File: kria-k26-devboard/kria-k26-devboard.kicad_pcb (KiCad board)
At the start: 2 copper layers, 6 parts, among them J1 ADM6-60-01.5-L-4-2-A-TR, J2 ADM6-60-01.5-L-4-2-A-TR

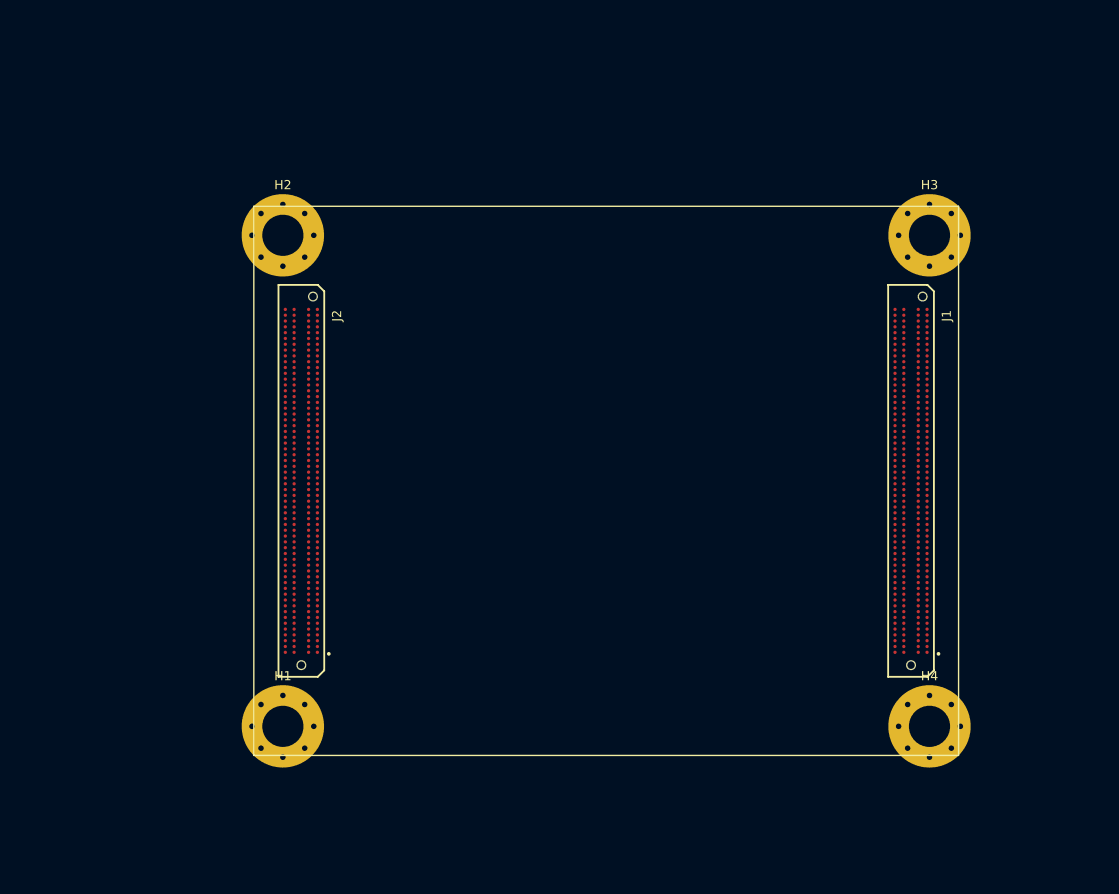
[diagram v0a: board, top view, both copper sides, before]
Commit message: Add dummy connectors for mechanical mockup purpouses
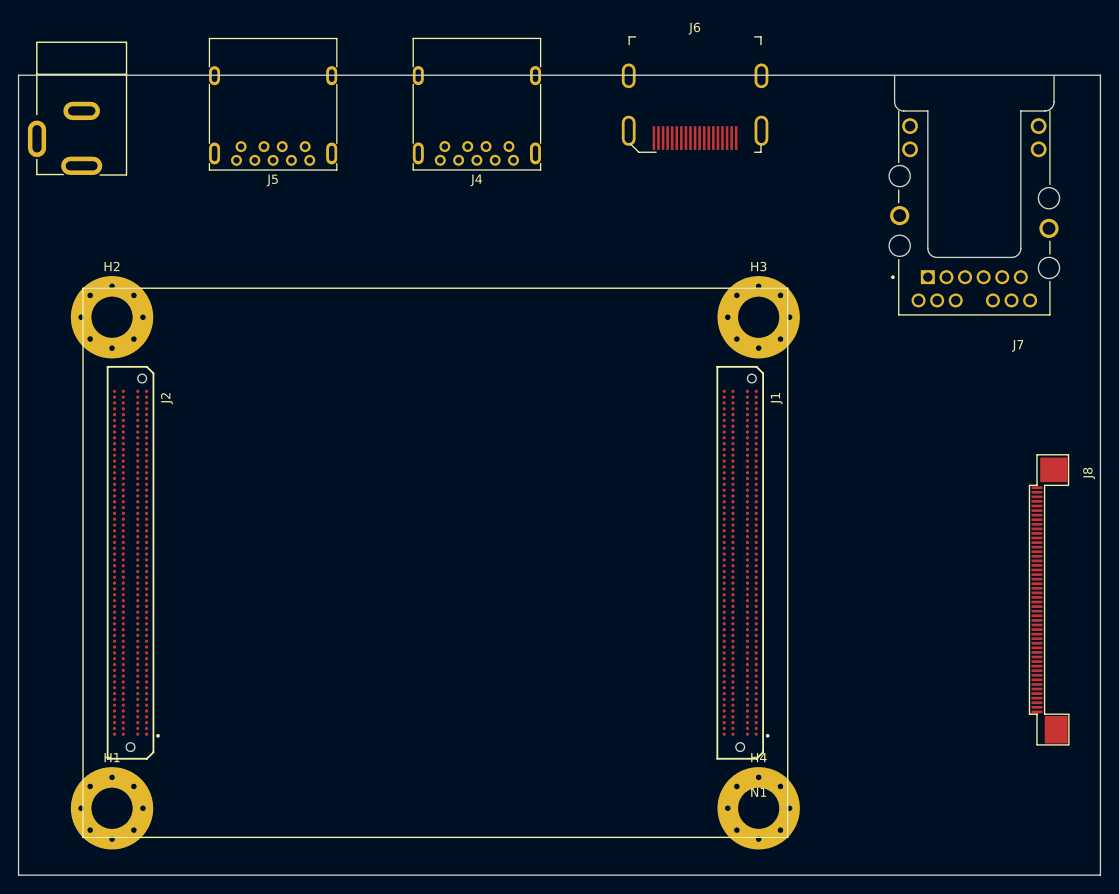
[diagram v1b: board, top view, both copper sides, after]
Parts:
- added J3: DC_SOCKET, antmicro-footprints:DC_SOCKET, F.Cu at (85.8, 43.6)
- added J4: 48393-0001, antmicro-footprints:48393-001, F.Cu at (132.5, 55.2)
- added J5: 48393-0001, antmicro-footprints:48393-001, F.Cu at (110.2, 55.2)
- added J6: 685119134923_, antmicro-footprints:HDMI_A_Female_685119134923, F.Cu at (152.8, 53.0)
- added J7: L834-1G1T-S7, antmicro-footprints:BEL_L834-1G1T-S7, F.Cu at (183.3, 62.8)
- added J8: WE_68715014022, antmicro-footprints:WE_68715014022, F.Cu at (190.8, 105.4)
- added N1: Housing, Fiducial:Fiducial_0.5mm_Mask1.5mm, F.Cu at (159.8, 127.5)
- moved H1 20.7 mm to (89.1, 127.5)
- moved H2 20.7 mm to (89.1, 73.9)
- moved J2 20.7 mm to (91.1, 100.7)
- moved H3 20.7 mm to (159.8, 73.9)
- moved H4 20.7 mm to (159.8, 127.5)
- moved J1 20.7 mm to (157.7, 100.7)
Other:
- board outline added: 118.2 x 87.4 mm

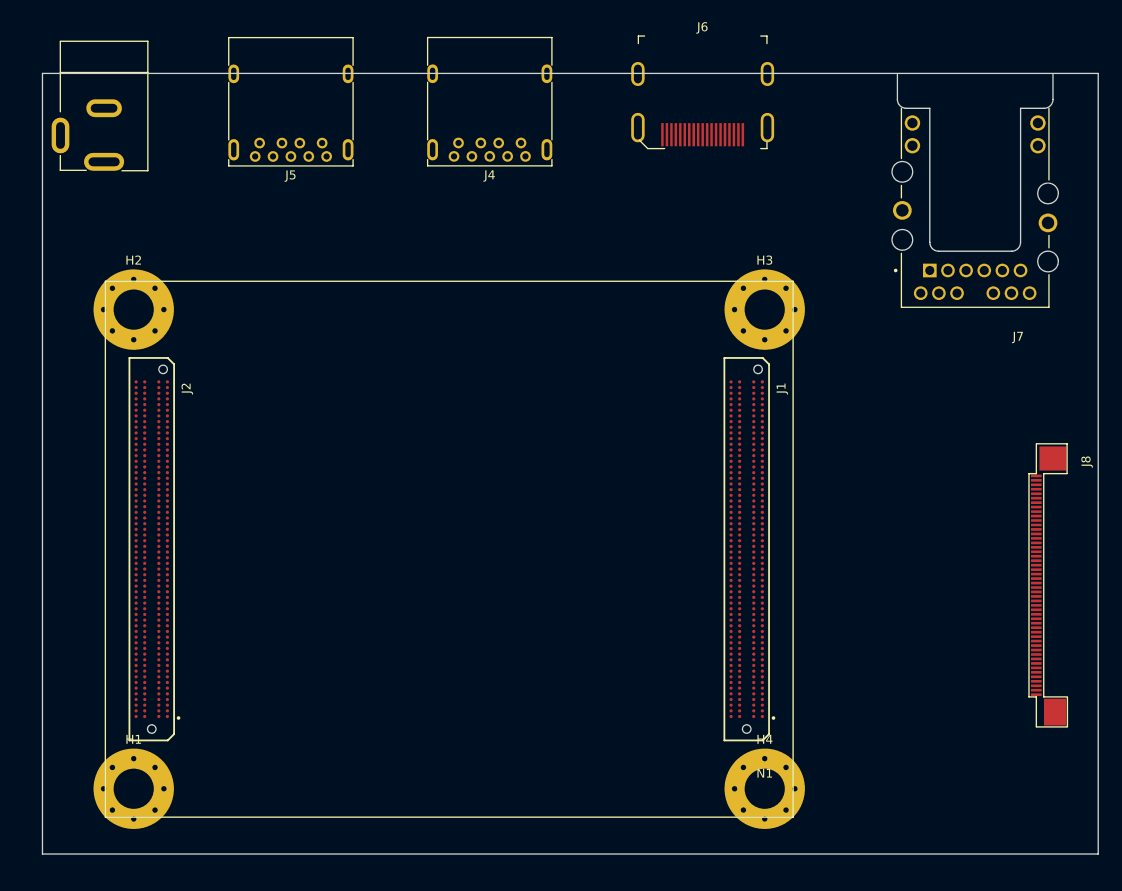
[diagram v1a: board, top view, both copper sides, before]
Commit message: Replace K26 SOM with virtual component
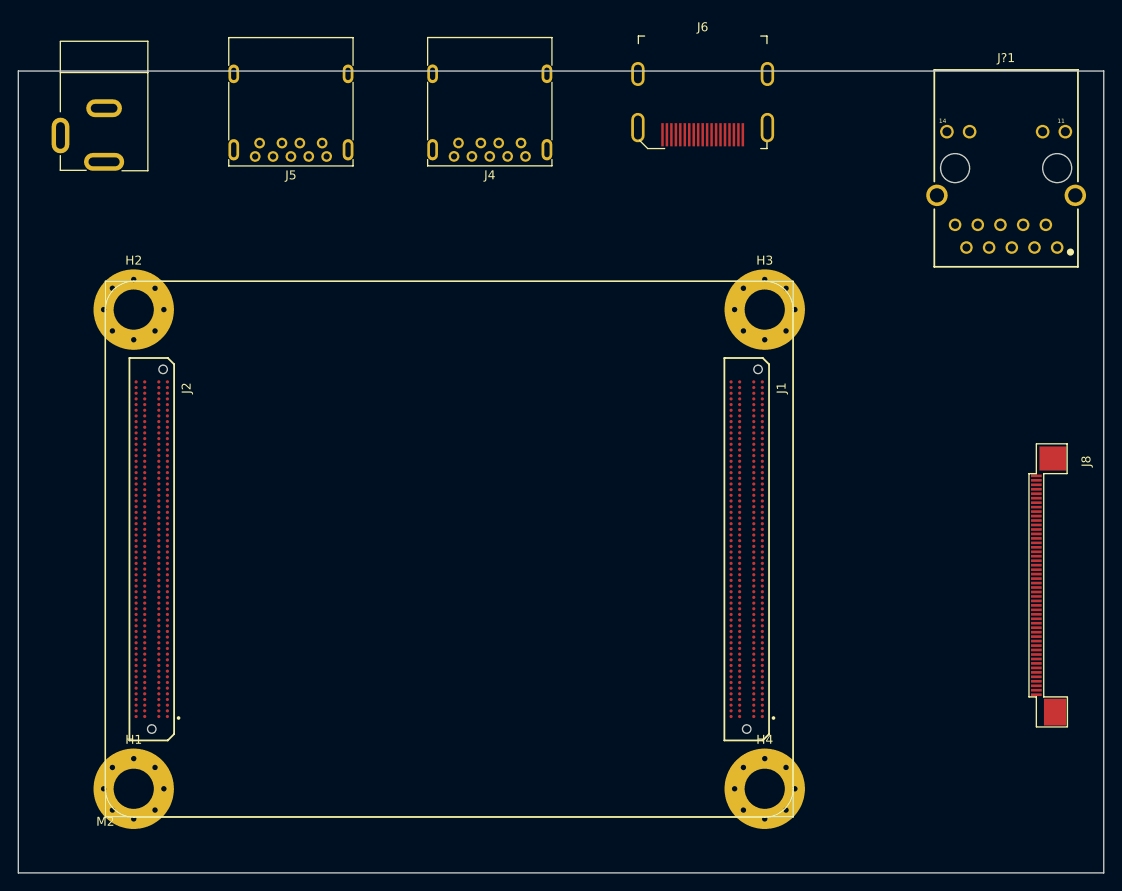
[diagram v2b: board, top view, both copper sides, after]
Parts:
- removed J7: L834-1G1T-S7, antmicro-footprints:BEL_L834-1G1T-S7
- removed N1: Housing, Fiducial:Fiducial_0.5mm_Mask1.5mm
- added J?1: WE-RJ45_7499111121A, antmicro-footprints:7499111121A, F.Cu at (186.8, 58.0)
- added M2: XILINX-KRIA-K26, antmicro-footprints:XILINX-KRIA-K26, F.Cu at (85.9, 130.7)
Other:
- board size 118.2 x 87.4 mm -> 121.5 x 89.8 mm

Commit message: First sketches of POE part of supply
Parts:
- removed H1, H2, H3, H4: MountingHole_Pad, MountingHole:MountingHole_4.5mm_Pad_Via
- removed J8: WE_68715014022, antmicro-footprints:WE_68715014022
- removed J?1: WE-RJ45_7499111121A, antmicro-footprints:7499111121A
- removed M2: XILINX-KRIA-K26, antmicro-footprints:XILINX-KRIA-K26
- added C1: C_47u_0805, antmicro-footprints:0805-cap, F.Cu at (293.3, 60.4)
- added C2: C_47u_0805, antmicro-footprints:0805-cap, F.Cu at (215.0, 114.6)
- added C3: C_1u_0402, antmicro-footprints:0402-cap, F.Cu at (214.1, 117.1)
- added C4: C_100n_0402, antmicro-footprints:0402-cap, F.Cu at (218.9, 114.2)
- added J7: WE_68715014022, antmicro-footprints:WE_68715014022, F.Cu at (366.2, 49.5)
- added J_SOM240_1: ADM6-60-01.5-L-4-2-A-TR, antmicro-footprints:SAMTEC_ADM6-60-01.5-L-4-2-A-TR, F.Cu at (218.6, 75.5)
- added J_SOM240_2: ADM6-60-01.5-L-4-2-A-TR, antmicro-footprints:SAMTEC_ADM6-60-01.5-L-4-2-A-TR, F.Cu at (285.1, 75.5)
- added M1: XILINX-KRIA-K26, antmicro-footprints:XILINX-KRIA-K26, F.Cu at (213.4, 105.5)
- added SP1: JSOM-0515-01, antmicro-footprints:SAMTEC_JSOM-0515-01, F.Cu at (208.6, 100.8)
- added SP2: JSOM-0515-01, antmicro-footprints:SAMTEC_JSOM-0515-01, F.Cu at (338.8, 48.4)
- added SP3: JSOM-0515-01, antmicro-footprints:SAMTEC_JSOM-0515-01, F.Cu at (294.4, 55.4)
- added SP4: JSOM-0515-01, antmicro-footprints:SAMTEC_JSOM-0515-01, F.Cu at (260.5, 109.7)
- J1: value ADM6-60-01.5-L-4-2-A-TR -> WE-RJ45_7499111121A; footprint antmicro-footprints:SAMTEC_ADM6-60-01.5-L-4-2-A-TR -> antmicro-footprints:7499111121A
- J2: value ADM6-60-01.5-L-4-2-A-TR -> DC_SOCKET; footprint antmicro-footprints:SAMTEC_ADM6-60-01.5-L-4-2-A-TR -> antmicro-footprints:DC_SOCKET
- J3: value DC_SOCKET -> USB4105-GF-A; footprint antmicro-footprints:DC_SOCKET -> antmicro-footprints:GCT_USB4105-GF-A
- moved J2 264.6 mm to (355.2, 83.8), turned to 0 degrees
- moved J3 180.3 mm to (-91.4, 76.9), turned to 0 degrees
- moved J6 173.7 mm to (306.8, 133.4)
- moved J5 170.6 mm to (265.2, 126.5), turned to 0 degrees
- moved J4 165.0 mm to (281.2, 126.5), turned to 0 degrees
- moved J1 72.7 mm to (222.0, 134.6), turned to 0 degrees

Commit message: Finished PoE part and DC-DC for PS and PL domains
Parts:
- added C10: C_100n_0805_100V, antmicro-footprints:0805-cap, F.Cu at (77.2, 0.09)
- added C11: C_100n_0805_100V, antmicro-footprints:0805-cap, F.Cu at (82.1, -2.82)
- added C12: C_47u_ELEC_100V, antmicro-footprints:CP_Elec_10x10.5, F.Cu at (59.1, -10.3)
- added C13: C_1n0_0402, antmicro-footprints:0402-cap, F.Cu at (67.8, 6.18)
- added C14: C_47u_ELEC_100V, antmicro-footprints:CP_Elec_10x10.5, F.Cu at (59.1, 1.75)
- added C15: C_47u_ELEC_100V, antmicro-footprints:CP_Elec_10x10.5, F.Cu at (73.7, -10.3)
- added C16: C_47u_16V_1206, antmicro-footprints:1206-cap, F.Cu at (55.6, 16.0)
- added C17: C_47u_16V_1206, antmicro-footprints:1206-cap, F.Cu at (47.5, 12.3)
- added C18: C_100n_0402_16V, antmicro-footprints:0402-cap, F.Cu at (82.3, -10.4)
- added C5: C_47u_0805, antmicro-footprints:0805-cap, F.Cu at (210.3, 35.4)
- added C6: C_47u_0805, antmicro-footprints:0805-cap, F.Cu at (215.2, 35.4)
- added C7: C_1u_0402, antmicro-footprints:0402-cap, F.Cu at (209.4, 37.9)
- added C8: C_100n_0402, antmicro-footprints:0402-cap, F.Cu at (212.3, 37.9)
- added C9: C_100n_0805_100V, antmicro-footprints:0805-cap, F.Cu at (68.7, 3.73)
- added D1: MB10S, antmicro-footprints:MB10S, F.Cu at (56.9, 11.0)
- added D2: MB10S, antmicro-footprints:MB10S, F.Cu at (39.5, 13.9)
- added D3: 1N4448, Diode_THT:D_DO-35_SOD27_P7.62mm_Horizontal, F.Cu at (25.2, 12.4)
- added D4: SMAJ58A-13-F, antmicro-footprints:DO-214AC, F.Cu at (27.6, 16.3)
- added D5: SMAJ58A-13-F, antmicro-footprints:DO-214AC, F.Cu at (48.2, 16.4)
- added IC1: TPS2378DDA, antmicro-footprints:SOIC127P600X170-9N, F.Cu at (70.5, -1.00)
- added PS1: PDQE30-Q48-S12-D, antmicro-footprints:PDQE30-Q48, F.Cu at (177.8, 88.0)
- added Q1: PJA3441, antmicro-footprints:SOT-23-3, F.Cu at (83.2, -13.8)
- added R1: R_2M2_0805, antmicro-footprints:0805-res, F.Cu at (77.2, -2.82)
- added R2: R_24k9_0402, antmicro-footprints:0402-res, F.Cu at (72.6, 3.27)
- added R3: R_63R4_0402, antmicro-footprints:0402-res, F.Cu at (82.3, -8.39)
- added R4: R_100k_0805, antmicro-footprints:0805-res, F.Cu at (61.3, 16.5)
- added U1: FT4232HPQ, antmicro-footprints:QFN-68_EP_8x8_Pitch0.4mm, F.Cu at (25.9, 55.3)
- added U2: TPSM84209, antmicro-footprints:TPSM84209RKHx, F.Cu at (37.3, 24.9)
- added U3: MAX5984AETI+T, antmicro-footprints:Maxim_MAX5984_TQFN-EP-28, F.Cu at (65.2, 11.4)
- moved J7 267.6 mm to (105.7, -11.7)
- moved SP2 217.9 mm to (156.3, 167.5)
- moved SP3 168.0 mm to (163.4, 160.4)
- moved J_SOM240_1 134.8 mm to (86.6, 103.2)
- moved J_SOM240_2 134.8 mm to (153.2, 103.2)
- moved M1 134.8 mm to (81.4, 133.2)
- moved J3 118.7 mm to (26.8, 66.3)
- moved SP1 79.3 mm to (156.3, 160.4)
- moved SP4 41.2 mm to (301.4, 104.4)
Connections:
- J3 pad A5: Net-(J3-PadA5) -> /Debug/PD_CC1
- J3 pad B5: Net-(J3-PadB5) -> /Debug/PD_CC2
- J_SOM240_1 pad B49: /Xilinx K26 SOM/GTR_REFCLK1_C2M_P -> /Xilinx K26 SOM/REFCLK1_C2M_P
- J_SOM240_1 pad C47: /Xilinx K26 SOM/GTR_DP0_M2C_N -> /Xilinx K26 SOM/GTR_REFCLK0_C2M_P
- J_SOM240_1 pad C48: /Xilinx K26 SOM/GTR_DP0_M2C_P -> /Xilinx K26 SOM/GTR_REFCLK0_C2M_N
- J_SOM240_1 pad C51: /Xilinx K26 SOM/GTR_DP2_C2M_N -> /Xilinx K26 SOM/GTR_DP3_M2C_P
- J_SOM240_1 pad C52: /Xilinx K26 SOM/GTR_DP2_C2M_P -> /Xilinx K26 SOM/GTR_DP3_M2C_N
- J_SOM240_1 pad C55: /Xilinx K26 SOM/REFCLK1_C2M_N -> /Xilinx K26 SOM/GTR_DP1_C2M_P
- J_SOM240_1 pad C56: /Xilinx K26 SOM/GTR_REFCLK1_C2M_P -> /Xilinx K26 SOM/GTR_DP1_C2M_N
- J_SOM240_1 pad D49: /Xilinx K26 SOM/GTR_DP0_M2C_P -> /Xilinx K26 SOM/GTR_DP3_C2M_P
- J_SOM240_1 pad D50: /Xilinx K26 SOM/GTR_DP0_M2C_N -> /Xilinx K26 SOM/GTR_DP3_C2M_N
- J_SOM240_1 pad D53: /Xilinx K26 SOM/GTR_DP0_M2C_P -> /Xilinx K26 SOM/GTR_REFCLK2_C2M_P
- J_SOM240_1 pad D54: /Xilinx K26 SOM/GTR_DP0_M2C_N -> /Xilinx K26 SOM/GTR_REFCLK2_C2M_N
- J_SOM240_1 pad D57: /Xilinx K26 SOM/GTR_DP0_M2C_P -> /Xilinx K26 SOM/GTR_DP2_M2C_P
- J_SOM240_1 pad D58: /Xilinx K26 SOM/GTR_DP0_M2C_N -> /Xilinx K26 SOM/GTR_DP2_M2C_N
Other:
- copper layers 2 -> 8

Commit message: Fixed VSS connection for OSC and LED pin in PoE POS section, first update of ETH schematic
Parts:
- added C19: C_10u_25V_0603, antmicro-footprints:0603-cap, F.Cu at (20.8, 98.2)
- added C20: C_10u_25V_0603, antmicro-footprints:0603-cap, F.Cu at (40.4, 79.6)
- added C21: C_10u_25V_0603, antmicro-footprints:0603-cap, F.Cu at (18.1, 95.8)
- added C22: C_10u_25V_0603, antmicro-footprints:0603-cap, F.Cu at (34.8, 82.1)
- added C23: C_10u_25V_0603, antmicro-footprints:0603-cap, F.Cu at (27.7, 85.3)
- added C24: C_100n_0402, antmicro-footprints:0402-cap, F.Cu at (34.2, 92.0)
- added C25: C_100n_0402, antmicro-footprints:0402-cap, F.Cu at (26.9, 99.5)
- added C26: C_100n_0402, antmicro-footprints:0402-cap, F.Cu at (40.3, 85.8)
- added C27: C_100n_0402, antmicro-footprints:0402-cap, F.Cu at (30.7, 96.5)
- added C28: C_100n_0402, antmicro-footprints:0402-cap, F.Cu at (38.7, 88.8)
- added C29: C_10u_25V_0603, antmicro-footprints:0603-cap, F.Cu at (18.1, 93.3)
- added C30: C_22u_0603, antmicro-footprints:0603-cap, F.Cu at (34.8, 84.5)
- added C31: C_22u_0603, antmicro-footprints:0603-cap, F.Cu at (13.7, 98.0)
- added C32: C_22u_0603, antmicro-footprints:0603-cap, F.Cu at (19.0, 90.8)
- added C33: C_22u_0603, antmicro-footprints:0603-cap, F.Cu at (23.7, 87.6)
- added C34: C_22u_0603, antmicro-footprints:0603-cap, F.Cu at (24.2, 85.0)
- added C35: C_22u_0603, antmicro-footprints:0603-cap, F.Cu at (27.7, 82.9)
- added C36: C_22u_0603, antmicro-footprints:0603-cap, F.Cu at (24.2, 82.5)
- added C37: C_22u_0603, antmicro-footprints:0603-cap, F.Cu at (29.7, 90.3)
- added C38: C_22u_0603, antmicro-footprints:0603-cap, F.Cu at (30.8, 87.8)
- added C39: C_22u_0603, antmicro-footprints:0603-cap, F.Cu at (33.3, 79.6)
- added C40: C_10u_25V_0603, antmicro-footprints:0603-cap, F.Cu at (31.3, 85.3)
- added C41: C_10u_25V_0603, antmicro-footprints:0603-cap, F.Cu at (26.1, 90.3)
- added C42: C_10u_25V_0603, antmicro-footprints:0603-cap, F.Cu at (25.2, 93.3)
- added C43: C_10u_25V_0603, antmicro-footprints:0603-cap, F.Cu at (21.6, 95.8)
- added C44: C_47u_0805, antmicro-footprints:0805-cap, F.Cu at (20.0, 84.9)
- added C45: C_47u_0805, antmicro-footprints:0805-cap, F.Cu at (24.7, 79.8)
- added C46: C_100n_0402, antmicro-footprints:0402-cap, F.Cu at (31.3, 94.5)
- added C47: C_100n_0402, antmicro-footprints:0402-cap, F.Cu at (24.8, 97.5)
- added C48: C_100n_0402, antmicro-footprints:0402-cap, F.Cu at (41.0, 81.8)
- added C49: C_22u_0603, antmicro-footprints:0603-cap, F.Cu at (27.3, 87.8)
- added C50: C_22u_0603, antmicro-footprints:0603-cap, F.Cu at (17.2, 98.2)
- added C51: C_22u_0603, antmicro-footprints:0603-cap, F.Cu at (36.8, 79.6)
- added C52: C_22u_0603, antmicro-footprints:0603-cap, F.Cu at (21.6, 93.3)
- added C53: C_22u_0603, antmicro-footprints:0603-cap, F.Cu at (22.6, 90.8)
- added C54: C_22u_0603, antmicro-footprints:0603-cap, F.Cu at (31.3, 82.9)
- added C55: C_100n_0402, antmicro-footprints:0402-cap, F.Cu at (58.8, 105.9)
- added C56: C_100n_0402, antmicro-footprints:0402-cap, F.Cu at (55.9, 105.9)
- added C57: C_100n_0402, antmicro-footprints:0402-cap, F.Cu at (53.0, 105.9)
- added C58: C_100n_0402, antmicro-footprints:0402-cap, F.Cu at (50.1, 105.9)
- added C59: C_100n_0402_50V, antmicro-footprints:0402-cap, F.Cu at (4.28, 114.3)
- added C60: C_100n_0402_50V, antmicro-footprints:0402-cap, F.Cu at (59.6, 79.4)
- added D10: ESD144B1W0201E6327XTSA1, antmicro-footprints:ESD144B1W0201E6327XTSA1, F.Cu at (62.1, 79.3)
- added D7: PESD2USB5UV-TR, antmicro-footprints:SOT-23s, F.Cu at (19.7, 111.2)
- added D8: PESD2USB5UV-TR, antmicro-footprints:SOT-23s, F.Cu at (19.7, 106.3)
- added D9: ESD144B1W0201E6327XTSA1, antmicro-footprints:ESD144B1W0201E6327XTSA1, F.Cu at (6.81, 114.2)
- added L1: XEL4030-222MEC, antmicro-footprints:Coilcraft-XEL4030, F.Cu at (5.50, 86.4)
- added L2: SRP2010-1R0M, antmicro-footprints:INDC2016X100N, F.Cu at (9.71, 98.4)
- added L3: SRP2010-1R0M, antmicro-footprints:INDC2016X100N, F.Cu at (9.71, 95.2)
- added L4: XEL4030-222MEC, antmicro-footprints:Coilcraft-XEL4030, F.Cu at (5.50, 81.0)
- added L5: SRP2010-1R0M, antmicro-footprints:INDC2016X100N, F.Cu at (29.3, 80.0)
- added L6: SRP2010-1R0M, antmicro-footprints:INDC2016X100N, F.Cu at (14.1, 95.2)
- added L7: SRP2010-1R0M, antmicro-footprints:INDC2016X100N, F.Cu at (19.8, 88.0)
- added L8: SRP2010-1R0M, antmicro-footprints:INDC2016X100N, F.Cu at (15.1, 90.1)
- added R10: R_12k4_0402, antmicro-footprints:0402-res, F.Cu at (37.1, 90.8)
- added R11: R_10k_0402, antmicro-footprints:0402-res, F.Cu at (34.2, 94.0)
- added R12: R_4k99_0402, antmicro-footprints:0402-res, F.Cu at (35.8, 88.8)
- added R13: R_10k_0402, antmicro-footprints:0402-res, F.Cu at (24.0, 99.5)
- added R14: R_2k49_0402, antmicro-footprints:0402-res, F.Cu at (41.0, 83.8)
- added R15: R_10k_0402, antmicro-footprints:0402-res, F.Cu at (38.1, 81.8)
- added R16: R_10k_0402, antmicro-footprints:0402-res, F.Cu at (37.4, 86.8)
- added R17: R_2k49_0402, antmicro-footprints:0402-res, F.Cu at (31.3, 92.5)
- added R18: R_31k6_0402, antmicro-footprints:0402-res, F.Cu at (32.9, 90.0)
- added R19: R_10k_0402, antmicro-footprints:0402-res, F.Cu at (38.1, 83.8)
- added R20: R_12k4_0402, antmicro-footprints:0402-res, F.Cu at (28.4, 94.5)
- added R21: R_10k_0402, antmicro-footprints:0402-res, F.Cu at (34.5, 86.8)
- added R22: R_4k99_0402, antmicro-footprints:0402-res, F.Cu at (28.4, 92.5)
- added R23: R_10k_0402, antmicro-footprints:0402-res, F.Cu at (24.8, 95.5)
- added R24: R_100R_0402, antmicro-footprints:0402-res, F.Cu at (47.2, 105.9)
- added R5: R_0R_0402, antmicro-footprints:0402-res, F.Cu at (27.7, 104.8)
- added R6: R_31k6_0402, antmicro-footprints:0402-res, F.Cu at (27.7, 96.5)
- added R7: R_10k_0402, antmicro-footprints:0402-res, F.Cu at (37.1, 92.7)
- added R8: R_21k5_0402, antmicro-footprints:0402-res, F.Cu at (33.6, 96.5)
- added R9: R_10k_0402, antmicro-footprints:0402-res, F.Cu at (29.8, 98.5)
- added U10: AP62301WU-7, antmicro-footprints:TSOT23-6, F.Cu at (5.17, 91.6)
- added U11: AP62301WU-7, antmicro-footprints:TSOT23-6, F.Cu at (10.5, 80.9)
- added U12: LTC4358CDE, antmicro-footprints:Linear_DFN-14, F.Cu at (53.6, 102.0)
- added U13: LTC4358CDE, antmicro-footprints:Linear_DFN-14, F.Cu at (58.9, 102.0)
- added U14: LTC4358CDE, antmicro-footprints:Linear_DFN-14, F.Cu at (48.4, 102.0)
- added U4: AP62301WU-7, antmicro-footprints:TSOT23-6, F.Cu at (15.2, 85.9)
- added U5: AP62301WU-7, antmicro-footprints:TSOT23-6, F.Cu at (10.5, 91.0)
- added U6: AP62301WU-7, antmicro-footprints:TSOT23-6, F.Cu at (19.9, 80.9)
- added U7: AP62301WU-7, antmicro-footprints:TSOT23-6, F.Cu at (10.5, 85.9)
- added U8: RPX-4.0-R, antmicro-footprints:Recom_15-PowerBQFN, F.Cu at (53.8, 134.7)
- added U9: AP62301WU-7, antmicro-footprints:TSOT23-6, F.Cu at (15.2, 80.9)
- D3: value 1N4448 -> 1N4448WS; footprint Diode_THT:D_DO-35_SOD27_P7.62mm_Horizontal -> Diode_SMD:D_SOD-323
- J2: value DC_SOCKET -> USB4105-GF-A; footprint antmicro-footprints:DC_SOCKET -> antmicro-footprints:GCT_USB4105-GF-A
- J3: value USB4105-GF-A -> DC_SOCKET; footprint antmicro-footprints:GCT_USB4105-GF-A -> antmicro-footprints:DC_SOCKET
- U2: value TPSM84209 -> AP62301WU-7; footprint antmicro-footprints:TPSM84209RKHx -> antmicro-footprints:TSOT23-6
- moved J2 347.7 mm to (8.45, 109.9)
- moved D3 127.6 mm to (67.8, 132.6)
- moved U2 78.6 mm to (5.17, 96.6)
- moved J3 37.5 mm to (51.8, 94.4)
- moved D4 3.62 mm to (30.6, 14.2)
- moved U3 3.62 mm to (68.1, 9.31)
- moved C10 3.62 mm to (80.2, -2.01)
- moved C12 3.62 mm to (62.1, -12.4)
- moved C13 3.62 mm to (70.7, 4.08)
- moved C14 3.62 mm to (62.1, -0.35)
- moved C15 3.62 mm to (76.7, -12.4)
- moved C17 3.62 mm to (50.5, 10.2)
- moved C18 3.62 mm to (85.3, -12.5)
- moved C9 3.62 mm to (71.7, 1.63)
- moved D1 3.62 mm to (59.9, 8.93)
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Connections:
- net /Power Supply/PoE/POE_5V renamed /Power Supply/PoE/POE_12V
- U2 pad 1: Net-(U2-Pad1) -> GND
- U2 pad 2: Net-(U2-Pad2) -> Net-(C24-Pad1)
- U2 pad 3: Net-(U2-Pad3) -> /Power Supply/DC/DC conventers/DC_MAIN_BUS
- U2 pad 4: Net-(U2-Pad4) -> Net-(R6-Pad2)
- U2 pad 5: Net-(U2-Pad4) -> /Power Supply/VCCOEN_PS_M2C
- U2 pad 6: (no net) -> Net-(C24-Pad2)
